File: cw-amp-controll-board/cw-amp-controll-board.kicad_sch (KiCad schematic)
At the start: 50 parts, among them J1 Conn_02x07_Odd_Even, J2 Conn_01x06, J3 Conn_02x05_Odd_Even, Q1 BC850, Q2 BC850, Q3 BC850, Q4 BC850, SW1 RotaryEncoder, U1 LDL1117S33R, U2 PCF8574, U3 ESP32-C3-WROOM-02, U4 AT42QT2120-CommsMode, U5 PCF8574

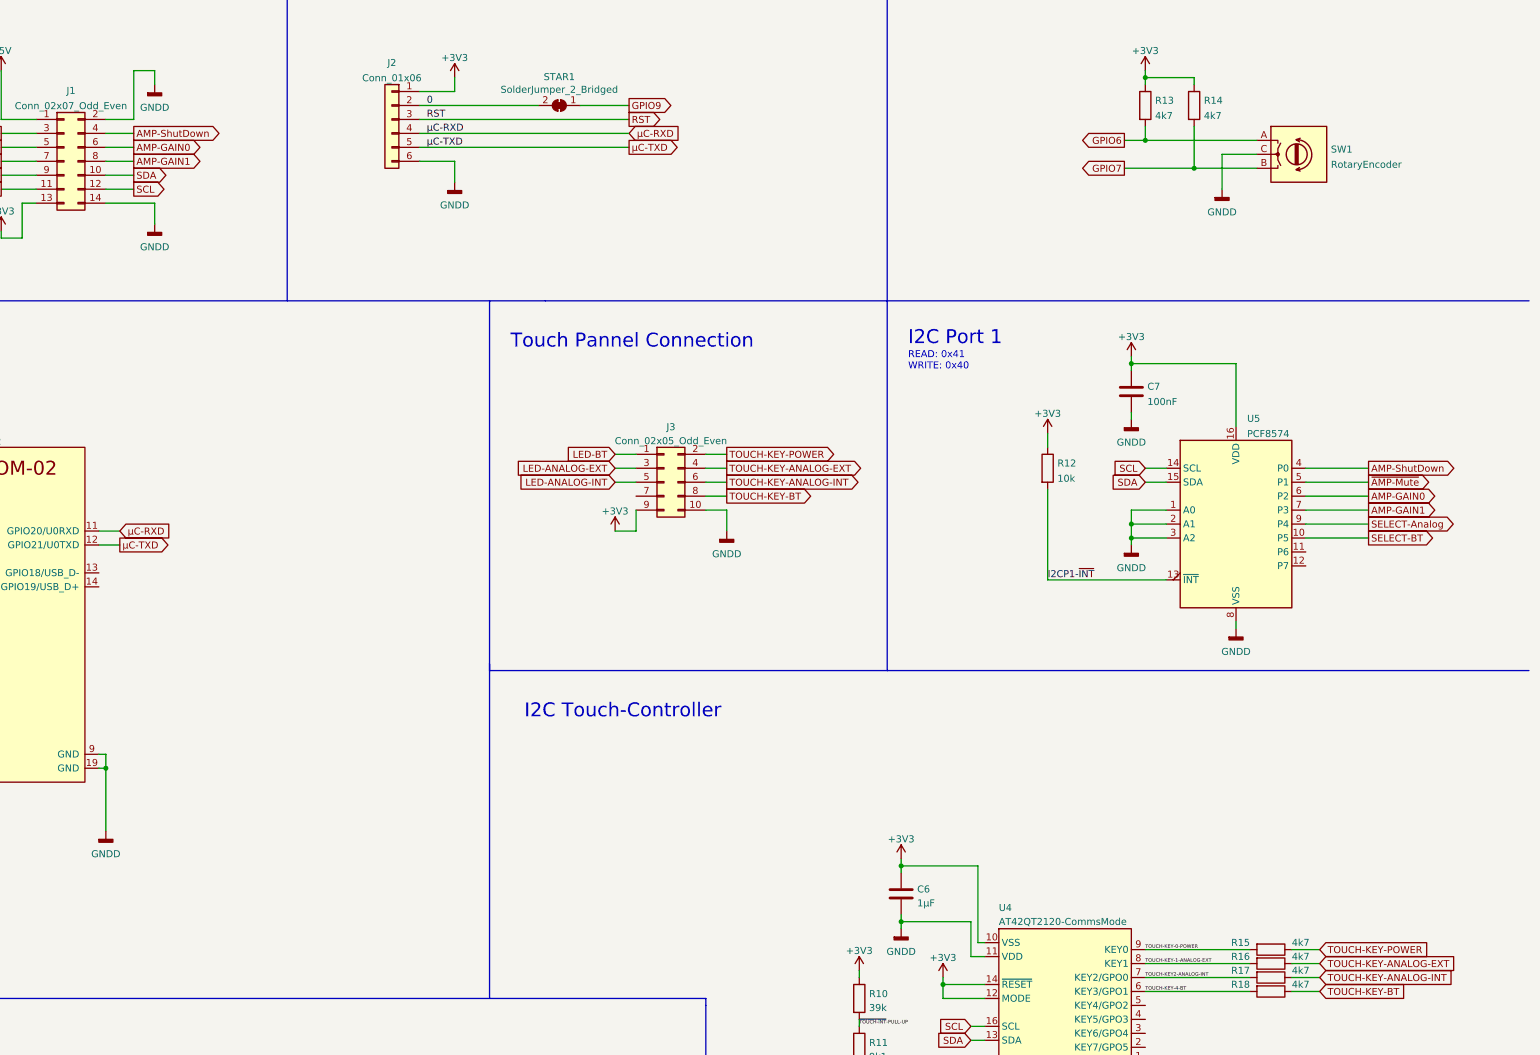
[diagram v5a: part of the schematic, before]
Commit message: removed errors control board, added interrupt pins controllboard
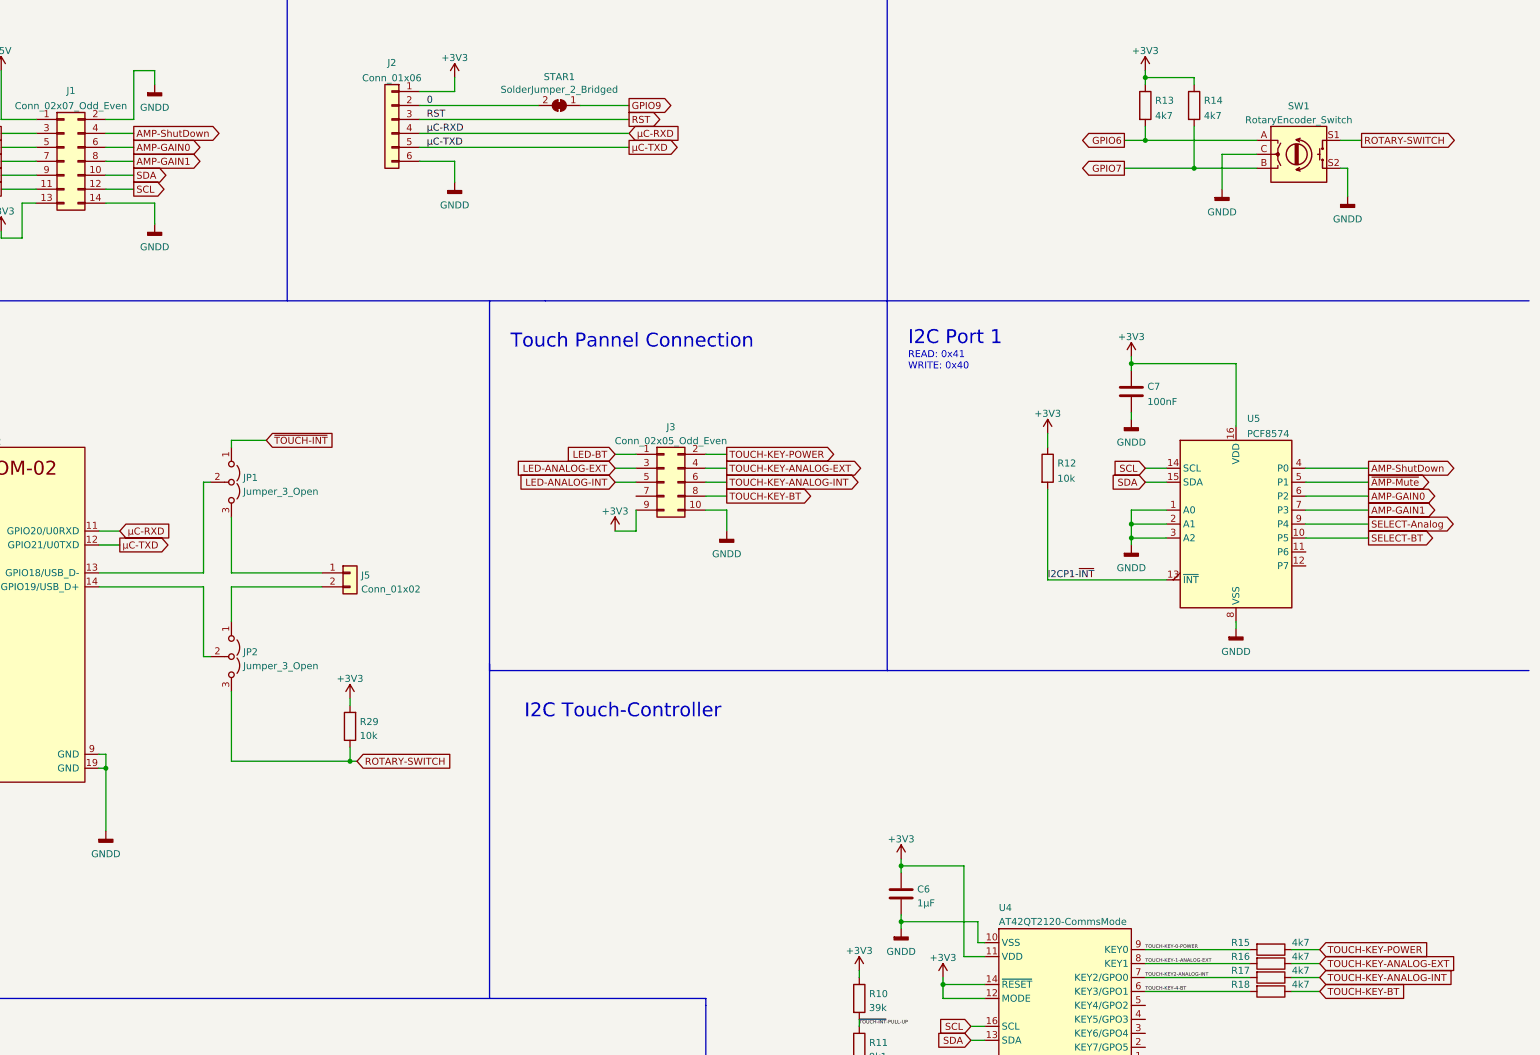
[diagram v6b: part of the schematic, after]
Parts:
- removed SW1: RotaryEncoder, office_amp:ALPS_STEC11B, symbol Device:RotaryEncoder
- added J5: Conn_01x02, Connector_PinHeader_2.54mm:PinHeader_1x02_P2.54mm_Vertical, symbol Connector_Generic:Conn_01x02
- added JP1, JP2: Jumper_3_Open, Jumper:SolderJumper-3_P1.3mm_Open_Pad1.0x1.5mm, symbol Jumper:Jumper_3_Open
- added R29: 10k, Resistor_SMD:R_0805_2012Metric_Pad1.20x1.40mm_HandSolder, symbol Device:R
- added SW1: RotaryEncoder_Switch, office_amp:ALPS_STEC11B, symbol Device:RotaryEncoder_Switch
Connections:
- net +3V3: now also U4.11 (VDD), R29.2; no longer U4.10 (VSS)
- net GNDD: now also U4.10 (VSS), SW1.C, SW1.S2; no longer U4.11 (VDD)
- net GPIO6: now also SW1.A
- net GPIO7: now also SW1.B
- net ~{TOUCH-INT}: now also JP1.1 (A)
- net at U3.13 (GPIO18/USB_D-): now also JP1.2 (C)
- net at U3.14 (GPIO19/USB_D+): now also JP2.2 (C)
- new net: J5.1 (Pin_1), JP1.3 (B)
- new net: J5.2 (Pin_2), JP2.1 (A)
- new net ROTARY-SWITCH: JP2.3 (B), R29.1, SW1.S1

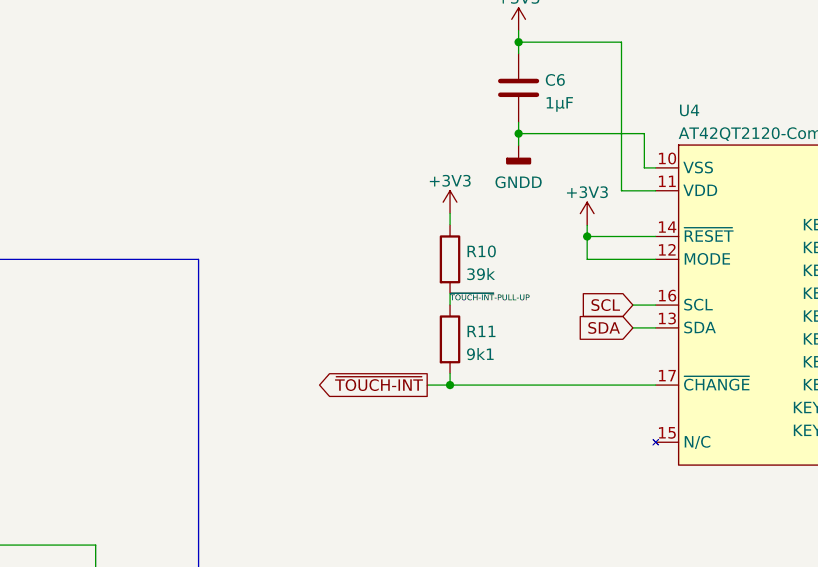
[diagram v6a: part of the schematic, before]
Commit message: error correction aftertest; corrected pinout touch; added level shifter for i2c poti; corrected voltages i2c poti
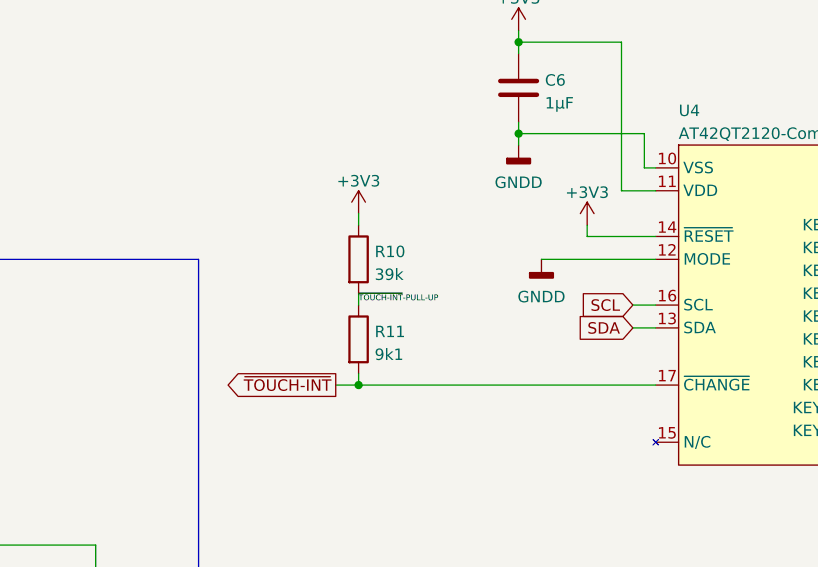
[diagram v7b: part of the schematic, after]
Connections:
- net +3V3: no longer U4.12 (MODE)
- net GNDD: now also U4.12 (MODE)
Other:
- moved on the sheet: R10, R11
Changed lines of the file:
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@@
   (junction (at 209.55 234.95) (diameter 0) (color 0 0 0 0)
   )
-  (junction (at 300.99 200.66) (diameter 0) (color 0 0 0 0)
-  )
   (junction (at 72.39 50.8) (diameter 0) (color 0 0 0 0)
   )
@@
   (junction (at 335.28 116.84) (diameter 0) (color 0 0 0 0)
   )
-  (junction (at 285.75 217.17) (diameter 0) (color 0 0 0 0)
+  (junction (at 275.59 217.17) (diameter 0) (color 0 0 0 0)
   )
   (junction (at 293.37 179.07) (diameter 0) (color 0 0 0 0)
@@
     (stroke (width 0) (type default) (color 0 0 0 0))
   )
-  (wire (pts (xy 285.75 215.9) (xy 285.75 217.17))
+  (wire (pts (xy 275.59 215.9) (xy 275.59 217.17))
     (stroke (width 0) (type default) (color 0 0 0 0))
   )
@@
     (stroke (width 0) (type default) (color 0 0 0 0))
   )
-  (wire (pts (xy 285.75 217.17) (xy 308.61 217.17))
+  (wire (pts (xy 275.59 217.17) (xy 308.61 217.17))
     (stroke (width 0) (type default) (color 0 0 0 0))
   )
@@
     (stroke (width 0) (type default) (color 0 0 0 0))
   )
-  (wire (pts (xy 285.75 198.12) (xy 285.75 199.39))
+  (wire (pts (xy 275.59 198.12) (xy 275.59 199.39))
     (stroke (width 0) (type default) (color 0 0 0 0))
   )
@@
     (stroke (width 0) (type default) (color 0 0 0 0))
   )
-  (wire (pts (xy 283.21 217.17) (xy 285.75 217.17))
+  (wire (pts (xy 273.05 217.17) (xy 275.59 217.17))
     (stroke (width 0) (type default) (color 0 0 0 0))
   )
@@
     (stroke (width 0) (type default) (color 0 0 0 0))
   )
-  (wire (pts (xy 300.99 203.2) (xy 308.61 203.2))
-    (stroke (width 0) (type default) (color 0 0 0 0))
-  )
   (wire (pts (xy 107.95 247.65) (xy 107.95 271.78))
     (stroke (width 0) (type default) (color 0 0 0 0))
@@
     (stroke (width 0) (type default) (color 0 0 0 0))
   )
-  (wire (pts (xy 285.75 207.01) (xy 285.75 208.28))
+  (wire (pts (xy 275.59 207.01) (xy 275.59 208.28))
     (stroke (width 0) (type default) (color 0 0 0 0))
   )
@@
     (stroke (width 0) (type default) (color 0 0 0 0))
   )
+  (wire (pts (xy 295.91 203.2) (xy 308.61 203.2))
+    (stroke (width 0) (type default) (color 0 0 0 0))
+  )
   (wire (pts (xy 337.82 106.68) (xy 341.63 106.68))
     (stroke (width 0) (type default) (color 0 0 0 0))
@@
     (stroke (width 0) (type default) (color 0 0 0 0))
   )
-  (wire (pts (xy 300.99 200.66) (xy 300.99 203.2))
-    (stroke (width 0) (type default) (color 0 0 0 0))
-  )
   (wire (pts (xy 88.9 118.11) (xy 92.71 118.11))
     (stroke (width 0) (type default) (color 0 0 0 0))
@@
     (effects (font (size 0.64 0.64)) (justify left bottom))
   )
-  (label "~{TOUCH-INT}-PULL-UP" (at 285.75 208.0697 0)
+  (label "~{TOUCH-INT}-PULL-UP" (at 275.59 208.0697 0)
     (effects (font (size 0.64 0.64)) (justify left bottom))
   )
@@
     )
   )
-  (global_label "~{TOUCH-INT}" (shape output) (at 283.21 217.17 180) (fields_autoplaced)
+  (global_label "~{TOUCH-INT}" (shape output) (at 273.05 217.17 180) (fields_autoplaced)
     (effects (font (size 1.27 1.27)) (justify right))
-    (property "Intersheet References" "${INTERSHEET_REFS}" (id 0) (at 270.0926 217.0906 0)
+    (property "Intersheet References" "${INTERSHEET_REFS}" (id 0) (at 259.9326 217.0906 0)
       (effects (font (size 1.27 1.27)) (justify right) hide)
     )
@@
     (pin "9")
   )
-  (symbol (lib_id "power:+3V3") (at 285.75 198.12 0) (unit 1)
+  (symbol (lib_id "power:+3V3") (at 275.59 198.12 0) (unit 1)
     (in_bom yes) (on_board yes) (fields_autoplaced)
-    (property "Reference" "#PWR033" (id 0) (at 285.75 201.93 0)
+    (property "Reference" "#PWR033" (id 0) (at 275.59 201.93 0)
       (effects (font (size 1.27 1.27)) hide)
     )
-    (property "Value" "+3V3" (id 1) (at 285.75 194.5155 0))
-    (property "Footprint" "" (id 2) (at 285.75 198.12 0)
+    (property "Value" "+3V3" (id 1) (at 275.59 194.5155 0))
+    (property "Footprint" "" (id 2) (at 275.59 198.12 0)
       (effects (font (size 1.27 1.27)) hide)
     )
-    (property "Datasheet" "" (id 3) (at 285.75 198.12 0)
+    (property "Datasheet" "" (id 3) (at 275.59 198.12 0)
       (effects (font (size 1.27 1.27)) hide)
     )
@@
     (pin "1")
   )
+  (symbol (lib_id "power:GNDD") (at 295.91 203.2 0) (unit 1)
+    (in_bom yes) (on_board yes) (fields_autoplaced)
+    (property "Reference" "#PWR?" (id 0) (at 295.91 209.55 0)
+      (effects (font (size 1.27 1.27)) hide)
+    )
+    (property "Value" "GNDD" (id 1) (at 295.91 207.3815 0))
+    (property "Footprint" "" (id 2) (at 295.91 203.2 0)
+      (effects (font (size 1.27 1.27)) hide)
+    )
+    (property "Datasheet" "" (id 3) (at 295.91 203.2 0)
+      (effects (font (size 1.27 1.27)) hide)
+    )
+    (pin "1")
+  )
   (symbol (lib_id "power:GNDD") (at 293.37 190.5 0) (unit 1)
     (in_bom yes) (on_board yes) (fields_autoplaced)
@@
     (pin "2")
   )
-  (symbol (lib_id "Device:R") (at 285.75 203.2 0) (unit 1)
+  (symbol (lib_id "Device:R") (at 275.59 203.2 0) (unit 1)
     (in_bom yes) (on_board yes) (fields_autoplaced)
-    (property "Reference" "R10" (id 0) (at 287.528 202.3653 0)
+    (property "Reference" "R10" (id 0) (at 277.368 202.3653 0)
       (effects (font (size 1.27 1.27)) (justify left))
     )
-    (property "Value" "39k" (id 1) (at 287.528 204.9022 0)
+    (property "Value" "39k" (id 1) (at 277.368 204.9022 0)
       (effects (font (size 1.27 1.27)) (justify left))
     )
-    (property "Footprint" "Resistor_SMD:R_0805_2012Metric_Pad1.20x1.40mm_HandSolder" (id 2) (at 283.972 203.2 90)
+    (property "Footprint" "Resistor_SMD:R_0805_2012Metric_Pad1.20x1.40mm_HandSolder" (id 2) (at 273.812 203.2 90)
       (effects (font (size 1.27 1.27)) hide)
     )
-    (property "Datasheet" "~" (id 3) (at 285.75 203.2 0)
+    (property "Datasheet" "~" (id 3) (at 275.59 203.2 0)
       (effects (font (size 1.27 1.27)) hide)
     )
@@
     (pin "1")
   )
-  (symbol (lib_id "Device:R") (at 285.75 212.09 0) (unit 1)
+  (symbol (lib_id "Device:R") (at 275.59 212.09 0) (unit 1)
     (in_bom yes) (on_board yes) (fields_autoplaced)
-    (property "Reference" "R11" (id 0) (at 287.528 211.2553 0)
+    (property "Reference" "R11" (id 0) (at 277.368 211.2553 0)
       (effects (font (size 1.27 1.27)) (justify left))
     )
-    (property "Value" "9k1" (id 1) (at 287.528 213.7922 0)
+    (property "Value" "9k1" (id 1) (at 277.368 213.7922 0)
       (effects (font (size 1.27 1.27)) (justify left))
     )
-    (property "Footprint" "Resistor_SMD:R_0805_2012Metric_Pad1.20x1.40mm_HandSolder" (id 2) (at 283.972 212.09 90)
+    (property "Footprint" "Resistor_SMD:R_0805_2012Metric_Pad1.20x1.40mm_HandSolder" (id 2) (at 273.812 212.09 90)
       (effects (font (size 1.27 1.27)) hide)
     )
-    (property "Datasheet" "~" (id 3) (at 285.75 212.09 0)
+    (property "Datasheet" "~" (id 3) (at 275.59 212.09 0)
       (effects (font (size 1.27 1.27)) hide)
     )
@@
       (reference "#PWR0108") (unit 1) (value "GNDD") (footprint "")
     )
+    (path "/76defdcf-c5d8-4d7c-bfdc-2bfcaacce374"
+      (reference "#PWR?") (unit 1) (value "GNDD") (footprint "")
+    )
     (path "/c69b3723-8151-4cdf-9090-67c835ef0944"

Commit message: new test software
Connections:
- no-connect marks 0 -> 1
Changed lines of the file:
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@@
   (junction (at 293.37 179.07) (diameter 0) (color 0 0 0 0)
   )
+  (no_connect (at 245.11 111.76))
   (wire (pts (xy 205.74 38.1) (xy 212.09 38.1))
     (stroke (width 0) (type default) (color 0 0 0 0))
